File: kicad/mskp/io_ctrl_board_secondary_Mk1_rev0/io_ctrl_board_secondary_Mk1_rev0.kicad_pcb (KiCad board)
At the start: 2 copper layers, 13 parts, among them J1 OLED_128x64, J2 USB_C_Receptacle_USB2.0, J3 Conn_01x12_Socket, SW1 SW_Omron_B3FS, U1 MCP23017_SP

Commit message: More work on io_ctrl_board_secondary_Mk1_rev0 layout and schema
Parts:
- added Q1: 2N3904, Package_TO_SOT_THT:TO-92_Inline, F.Cu at (115.0, 76.8)
- added R8: 100K, Resistor_THT:R_Axial_DIN0204_L3.6mm_D1.6mm_P5.08mm_Horizontal, F.Cu at (110.3, 73.6)
- added REF**: MountingHole_2.2mm_M2_Pad_Via, MountingHole:MountingHole_2.2mm_M2_Pad_Via, F.Cu at (109.5, 56.2)
- added REF**: MountingHole_2.2mm_M2_Pad_Via, MountingHole:MountingHole_2.2mm_M2_Pad_Via, F.Cu at (141.6, 100.0)
- added REF**: MountingHole_2.2mm_M2_Pad_Via, MountingHole:MountingHole_2.2mm_M2_Pad_Via, F.Cu at (109.5, 100.1)
- added REF**: MountingHole_2.2mm_M2_Pad_Via, MountingHole:MountingHole_2.2mm_M2_Pad_Via, F.Cu at (141.6, 56.2)
- R1, R2, R3, R4: value Resistor -> 10k
- R5, R6, R7: value Resistor -> ?k
- moved R4 5.89 mm to (118.8, 97.5), turned to 180 degrees
- moved J2 3.57 mm to (112.4, 87.8)
- moved J3 3.33 mm to (136.8, 70.3)
- moved SW1 1.06 mm to (112.5, 65.4)
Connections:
- J2 pad A4: Net-(J1-VCC) -> Net-(Q1-C)
- J2 pad A9: Net-(J1-VCC) -> Net-(Q1-C)
- J2 pad B4: Net-(J1-VCC) -> Net-(Q1-C)
- J2 pad B9: Net-(J1-VCC) -> Net-(Q1-C)
- R4 pad 1: Net-(U1-~{RESET}) -> Net-(J1-VCC)
- R4 pad 2: Net-(J1-VCC) -> Net-(U1-~{RESET})
- SW1 pad 1: unconnected-(SW1-Pad1) -> Net-(Q1-B)
- SW1 pad 2: unconnected-(SW1-Pad2) -> Net-(D1-KB)

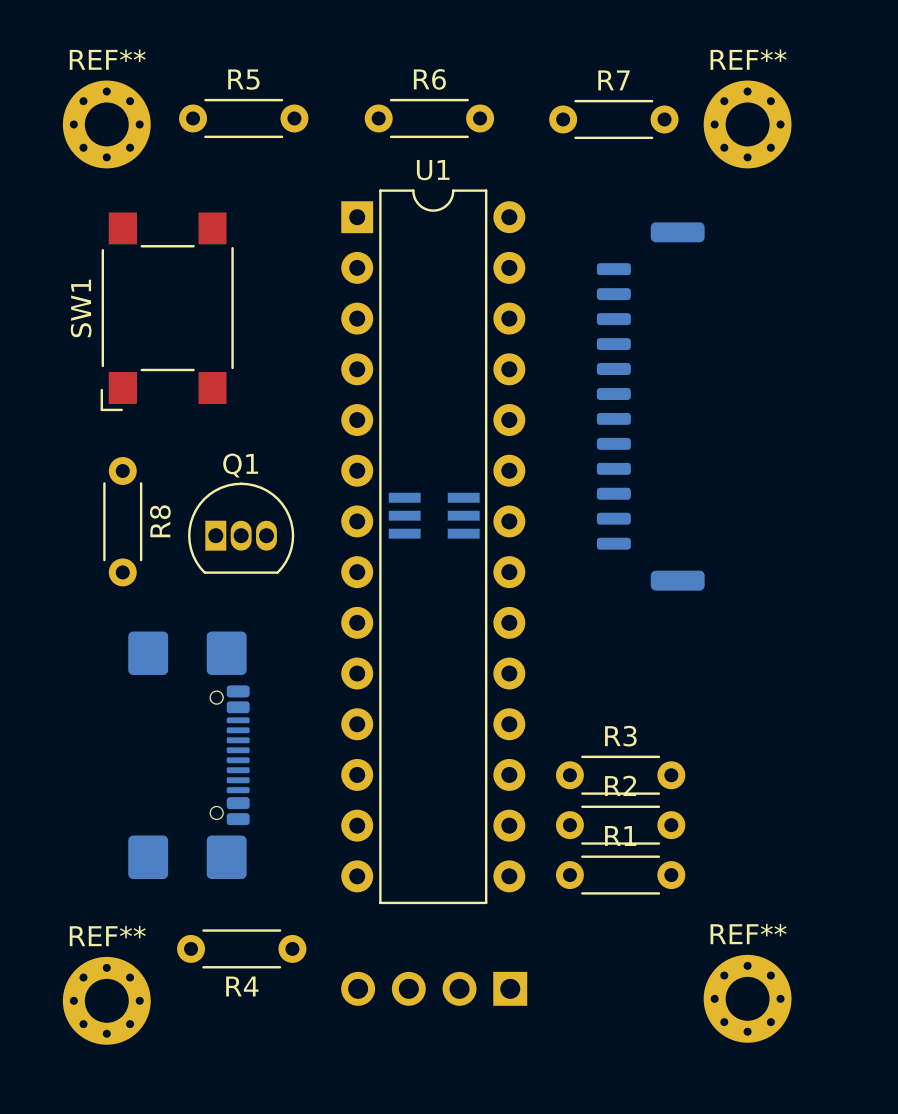
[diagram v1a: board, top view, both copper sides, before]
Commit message: Adds logo and OSH symbol to all mskp silkscreens
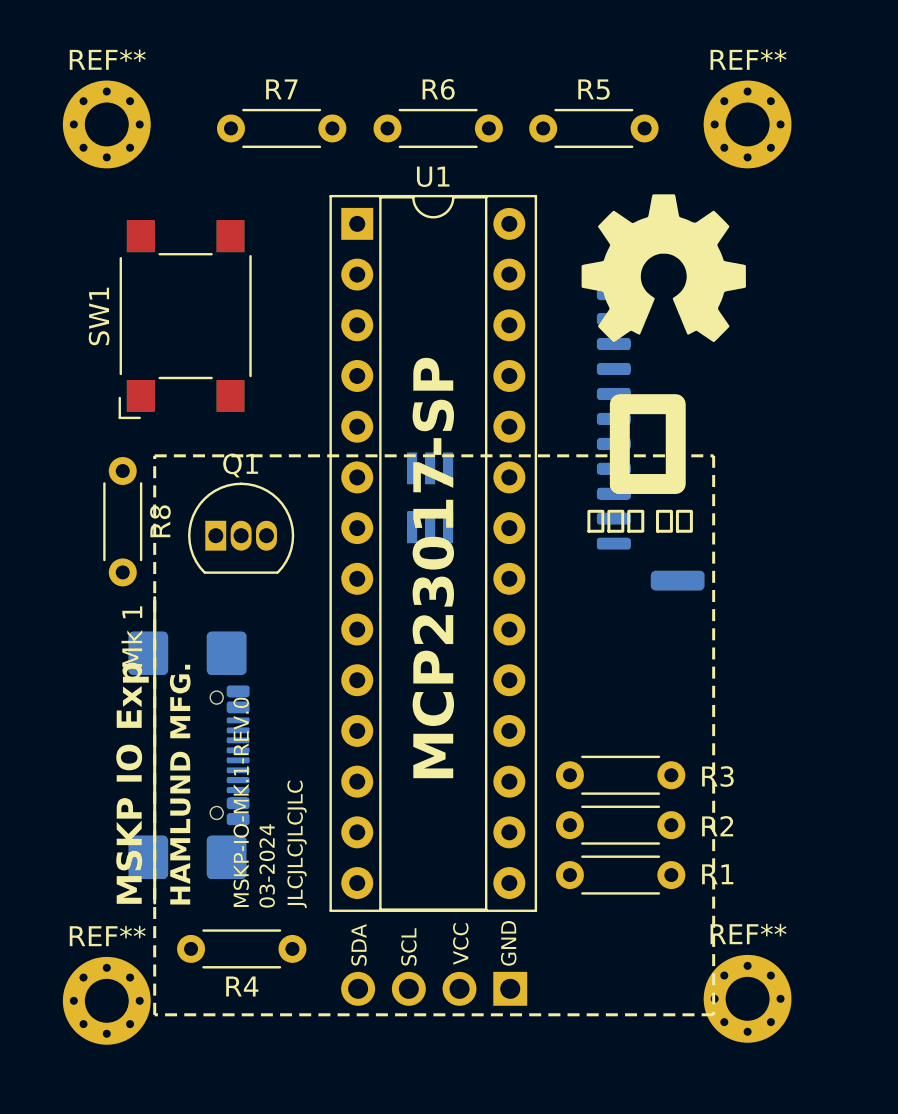
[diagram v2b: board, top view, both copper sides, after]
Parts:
- added G***: LOGO, Desktop:OSH_test, F.Cu at (137.4, 63.4)
- U1: footprint Package_DIP:DIP-28_W7.62mm -> Package_DIP:DIP-28_W7.62mm_Socket
- moved R5 17.5 mm to (131.4, 56.4)
- moved R7 16.6 mm to (115.7, 56.4)
- moved SW1 0.98 mm to (113.5, 65.8)
- moved D1 0.92 mm to (125.7, 74.9), turned to 90 degrees
- moved R6 0.67 mm to (123.6, 56.4)
- moved U1 0.34 mm to (122.0, 61.2)
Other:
- board text added: "03-2024"
- board text added: "GND"
- board text added: "HAMLUND MFG."
- board text added: "JLCJLCJLCJLC"
- board text added: "MCP23017-SP"
- board text added: "MSKP IO Exp"
- board text added: "MSKP-IO-MK.1-REV.0"
- board text added: "Mk 1"
- board text added: "SCL"
- board text added: "SDA"
- board text added: "VCC"
- board text added: "햄"
- board text added: "햄룬드 제조"

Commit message: Partial work on mskp part silkscreens
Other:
- board outline added: 38.3 x 50.2 mm
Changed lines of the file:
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@@
   (gr_line (start 111.9 79.9) (end 111.9 95.2)
     (stroke (width 0.15) (type default)) (layer "F.SilkS"))
+  (gr_line (start 106.2 100.7) (end 106.2 55.5)
+    (stroke (width 0.1) (type default)) (layer "Edge.Cuts"))
+  (gr_arc (start 144.5 100.7) (mid 143.767767 102.467767) (end 142 103.2)
+    (stroke (width 0.1) (type default)) (layer "Edge.Cuts"))
+  (gr_line (start 142 103.2) (end 108.7 103.2)
+    (stroke (width 0.1) (type default)) (layer "Edge.Cuts"))
+  (gr_arc (start 108.7 103.2) (mid 106.932233 102.467767) (end 106.2 100.7)
+    (stroke (width 0.1) (type default)) (layer "Edge.Cuts"))
+  (gr_arc (start 142 53) (mid 143.767767 53.732233) (end 144.5 55.5)
+    (stroke (width 0.1) (type default)) (layer "Edge.Cuts"))
+  (gr_line (start 108.7 53) (end 142 53)
+    (stroke (width 0.1) (type default)) (layer "Edge.Cuts"))
+  (gr_line (start 144.5 55.5) (end 144.5 100.7)
+    (stroke (width 0.1) (type default)) (layer "Edge.Cuts"))
+  (gr_arc (start 106.2 55.5) (mid 106.932233 53.732233) (end 108.7 53)
+    (stroke (width 0.1) (type default)) (layer "Edge.Cuts"))
   (gr_text "VCC" (at 127.7 98.3 90) (layer "F.SilkS")
     (effects (font (size 0.75 0.75) (thickness 0.15)) (justify left bottom))

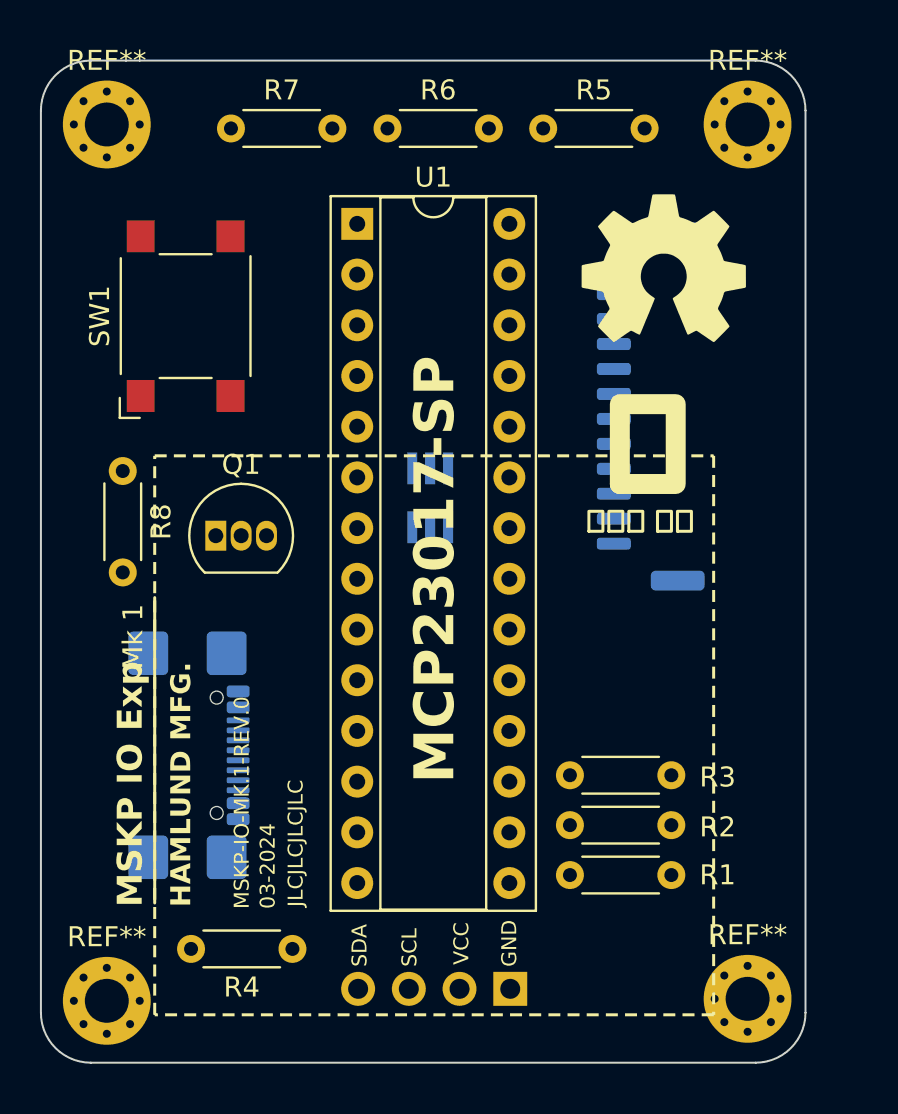
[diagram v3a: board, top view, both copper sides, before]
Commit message: Adds wiring for io_ctrl_board_secondary_Mk1_rev0
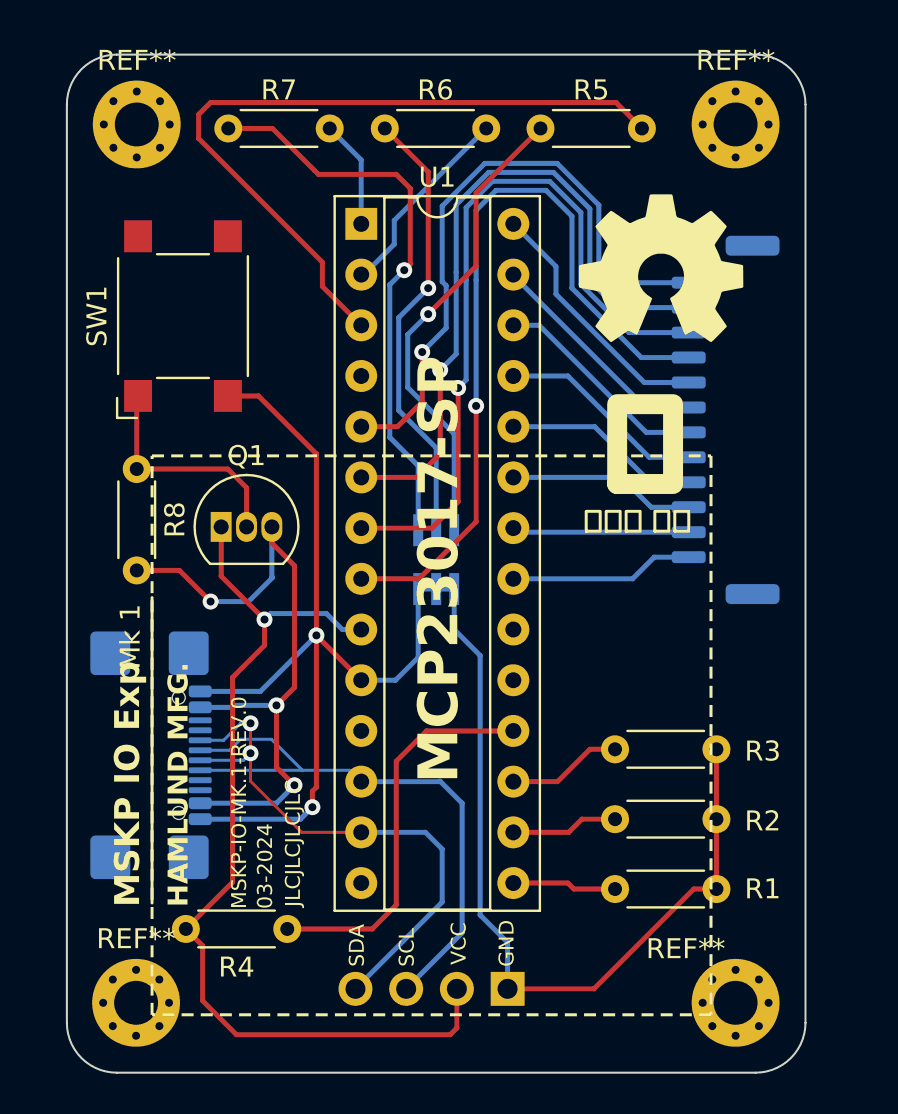
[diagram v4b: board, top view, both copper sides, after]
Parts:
- moved J3 3.81 mm to (140.5, 71.0)
- moved D1 3.11 mm to (126.0, 78.0)
- moved R3 2.61 mm to (135.0, 87.5)
- moved R1 2.37 mm to (135.0, 94.5)
- moved R2 2.28 mm to (135.0, 91.0)
- moved J2 1.90 mm to (110.5, 87.8)
- moved REF** 1.50 mm to (111.0, 56.2)
- moved REF** 1.47 mm to (111.0, 100.2)
- moved R4 1.03 mm to (118.5, 96.5)
- moved R8 0.71 mm to (111.0, 73.5)
- moved REF** 0.63 mm to (141.0, 100.2)
- moved REF** 0.60 mm to (141.0, 56.2)
- moved Q1 0.52 mm to (115.2, 76.4)
- moved U1 0.20 mm to (122.2, 61.2)
- moved G*** 0.13 mm to (137.3, 63.4)
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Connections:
- R4 pad 1: Net-(J1-VCC) -> Net-(U1-~{RESET})
- R4 pad 2: Net-(U1-~{RESET}) -> Net-(J1-VCC)
- R5 pad 2: Net-(U1-GPA7) -> Net-(U1-GPB2)
- R6 pad 2: Net-(U1-GPA6) -> Net-(U1-GPB1)
- R7 pad 2: Net-(U1-GPA5) -> Net-(U1-GPB0)
- U1 pad 1: Net-(J3-Pin_1) -> Net-(U1-GPB0)
- U1 pad 2: Net-(J3-Pin_2) -> Net-(U1-GPB1)
- U1 pad 21: Net-(J3-Pin_9) -> Net-(J3-Pin_12)
- U1 pad 22: Net-(J3-Pin_10) -> Net-(J3-Pin_11)
- U1 pad 23: Net-(J3-Pin_11) -> Net-(J3-Pin_10)
- U1 pad 24: Net-(J3-Pin_12) -> Net-(J3-Pin_9)
- U1 pad 25: unconnected-(U1-GPA4-Pad25) -> Net-(J3-Pin_8)
- U1 pad 26: Net-(U1-GPA5) -> Net-(J3-Pin_7)
- U1 pad 27: Net-(U1-GPA6) -> Net-(J3-Pin_6)
- U1 pad 28: Net-(U1-GPA7) -> Net-(J3-Pin_5)
- U1 pad 3: Net-(J3-Pin_3) -> Net-(U1-GPB2)
- U1 pad 4: Net-(J3-Pin_4) -> unconnected-(U1-GPB3-Pad4)
- U1 pad 5: Net-(J3-Pin_5) -> Net-(J3-Pin_1)
- U1 pad 6: Net-(J3-Pin_6) -> Net-(J3-Pin_2)
- U1 pad 7: Net-(J3-Pin_7) -> Net-(J3-Pin_3)
- U1 pad 8: Net-(J3-Pin_8) -> Net-(J3-Pin_4)
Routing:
- net Net-(D1-KB): track 0.00 -> 88.7 mm, vias 0 -> 2
- net Net-(J1-VCC): track 0.00 -> 47.5 mm, vias 0 -> 1
- net Net-(J3-Pin_4): track 0.00 -> 39.2 mm, vias 0 -> 1
- net Net-(J3-Pin_3): track 0.00 -> 37.2 mm, vias 0 -> 1
- net Net-(U1-GPB2): track 0.00 -> 36.9 mm
- net Net-(J3-Pin_2): track 0.00 -> 34.5 mm, vias 0 -> 1
- net Net-(Q1-C): track 0.00 -> 33.6 mm, vias 0 -> 3
- net Net-(J3-Pin_1): track 0.00 -> 31.8 mm, vias 0 -> 1
- net Net-(J1-SCL): track 0.00 -> 30.3 mm
- net Net-(D1-AR): track 0.00 -> 28.5 mm, vias 0 -> 1
- net Net-(J1-SDA): track 0.00 -> 28.2 mm, vias 0 -> 2
- net Net-(D1-AB): track 0.00 -> 23.8 mm, vias 0 -> 1
- net Net-(D1-AG): track 0.00 -> 22.4 mm, vias 0 -> 1
- net Net-(U1-~{RESET}): track 0.00 -> 19.7 mm
- net Net-(J3-Pin_5): track 0.00 -> 12.9 mm
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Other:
- board size 38.3 x 50.2 mm -> 37 x 51 mm

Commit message: Polishes silkscreen on io_ctrl_board_secondary_Mk1_rev0
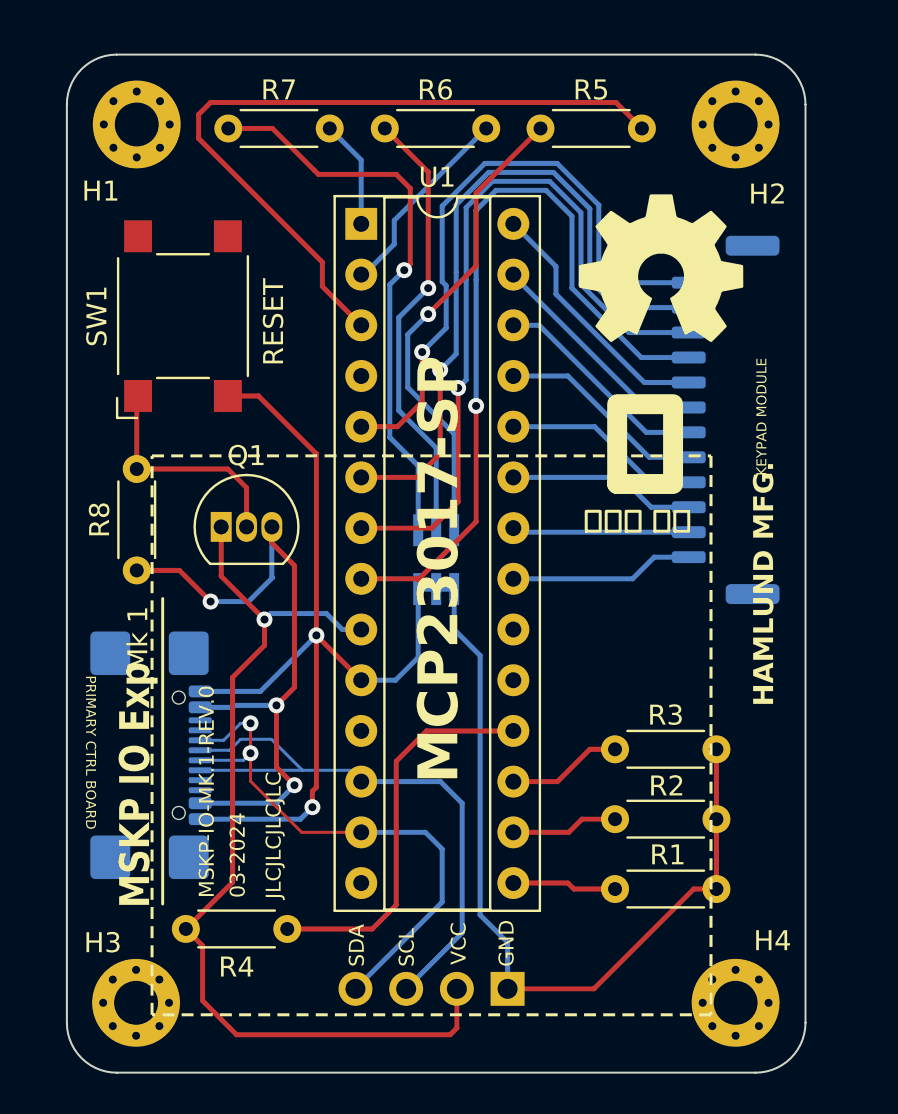
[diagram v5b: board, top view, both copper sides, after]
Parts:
- renumbered REF** to H1, REF** to H2, REF** to H3, REF** to H4
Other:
- board text added: "KEYPAD MODULE"
- board text added: "PRIMARY CTRL BOARD"
- board text added: "RESET"

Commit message: Cleans up unneeded files and adds more silkscreen tidy
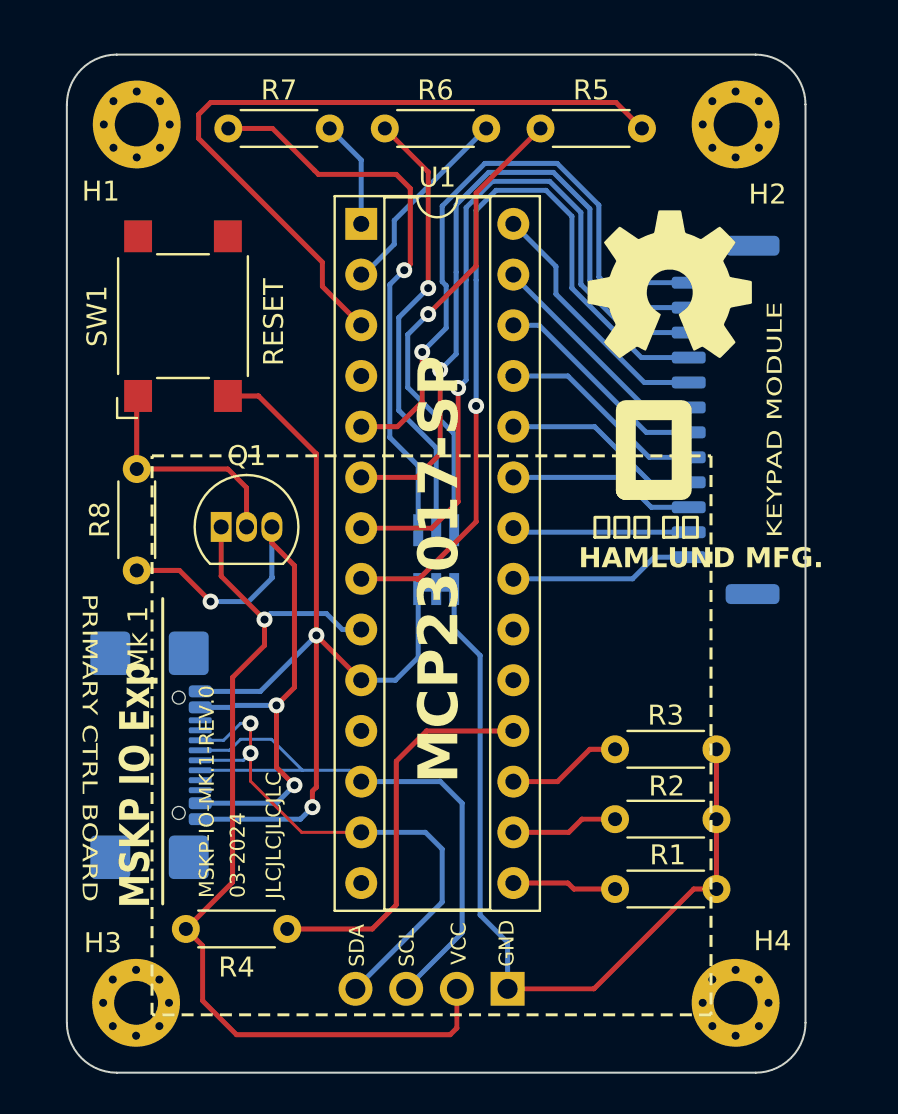
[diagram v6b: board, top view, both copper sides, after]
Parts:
- moved G*** 0.91 mm to (137.7, 64.2)

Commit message: Finalizes mskp pcbs before first run
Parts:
- moved J3 1.05 mm to (141.6, 71.0)
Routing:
- net Net-(J3-Pin_1): track 31.8 -> 32.8 mm
- net Net-(J3-Pin_9): track 9.94 -> 11.0 mm
- net Net-(J3-Pin_8): track 10.5 -> 11.5 mm
- net Net-(J3-Pin_7): track 11.0 -> 12.1 mm
- net Net-(J3-Pin_6): track 11.6 -> 12.6 mm
- net Net-(J3-Pin_5): track 12.9 -> 13.9 mm
- net Net-(J3-Pin_3): track 37.2 -> 38.3 mm
- net Net-(J3-Pin_2): track 34.5 -> 35.5 mm
- net Net-(J3-Pin_12): track 9.23 -> 10.3 mm
- net Net-(J3-Pin_11): track 8.87 -> 9.92 mm
- net Net-(J3-Pin_10): track 9.40 -> 10.5 mm
- net Net-(J3-Pin_4): track 39.2 -> 40.3 mm
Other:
- board text added: "IO Expander"
- board text removed: "MSKP IO Exp"
